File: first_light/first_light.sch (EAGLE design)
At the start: 20 parts, among them U1 STM32F051C6T6

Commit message: progress on schematic design
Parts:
- added C1, C2: (no value), rcl:C-EUC0603
- added C3, C4, C5: 100nF, rcl:C-EUC0603
- added IC1: MC34063AD, MC34063AD:MC34063AD
- added J1, J2: DCJ0202, con-jack:DCJ0202
- added JP1: PROG, pinhead:PINHD-1X5
- added LED1, LED2: (no value), led:LEDCHIP-LED0603
- added Q1: ZXMN4A06GTA, ZXMN4A06GTA:ZXMN4A06GTA
- added R14: 100R, rcl:R-EU_R0603
- added R15, R16: 10k, rcl:R-EU_R0603
- added R17, R18: 330, rcl:R-EU_R0603
- added S1: tact, SparkFun-Switches:MOMENTARY-SWITCH-SPST-PTH-6.0MM
- added S2: UP, SparkFun-Switches:MOMENTARY-SWITCH-SPST-PTH-6.0MM
- added S3: DOWN, SparkFun-Switches:MOMENTARY-SWITCH-SPST-PTH-6.0MM
- added S4: LEFT, SparkFun-Switches:MOMENTARY-SWITCH-SPST-PTH-6.0MM
- added S5: RIGHT, SparkFun-Switches:MOMENTARY-SWITCH-SPST-PTH-6.0MM
- added X1: 8MHz, IQD-Frequency-Products:CRYSTALS-NOGND-4-HSMX
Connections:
- new net !RST: JP1.1, S1.1, U1A.NRST
- new net +12V: J1.1, J2.1
- new net +3V3: C3.1, C4.1, C5.1, JP1.4, U1B.VDD, U1B.VDDA, U1B.VDD_2
- new net BTN_DN: S3.2, U1A.PA2
- new net BTN_L: S4.2, U1A.PA1
- new net BTN_R: S5.2, U1A.PA0
- new net BTN_UP: S2.2, U1A.PA3
- new net LED_ALM: R18.2, U1A.PA5
- new net LED_PWM: R14.1, R15.1
- new net LED_SET: R17.2, U1A.PA4
- new net N$14: C1.1, U1A.PF1-OSC_OUT, X1.1
- new net N$20: C2.1, U1A.PF0-OSC_IN, X1.2
- new net N$21: J2.2, J2.3, Q1.D_1, Q1.D_2
- new net N$23: Q1.G, R14.2
- new net N$24: LED2.A, R17.1
- new net N$25: R16.1, U1A.BOOT0
- new net N$26: LED1.A, R18.1
- new net SWCLK: JP1.3, U1A.PA14
- new net SWDIO: JP1.2, U1A.PA13
- net GND: now also C1.2, C2.2, C3.2, C4.2, C5.2, J1.2, J1.3, JP1.5, LED1.C, LED2.C, Q1.S, R15.2, R16.2, S1.2, S2.1, S3.1, S4.1, S5.1, U1B.VSS, U1B.VSSA, U1B.VSS_2
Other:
- note added: "Buck Converter"
- note added: "Display"
- note added: "LED Output"
- note added: "STM32"
- note added: "Supply"
- moved on the sheet: R1, R10, R11, R12, R13, R2, R3, R4, R5, R6, R7, R8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

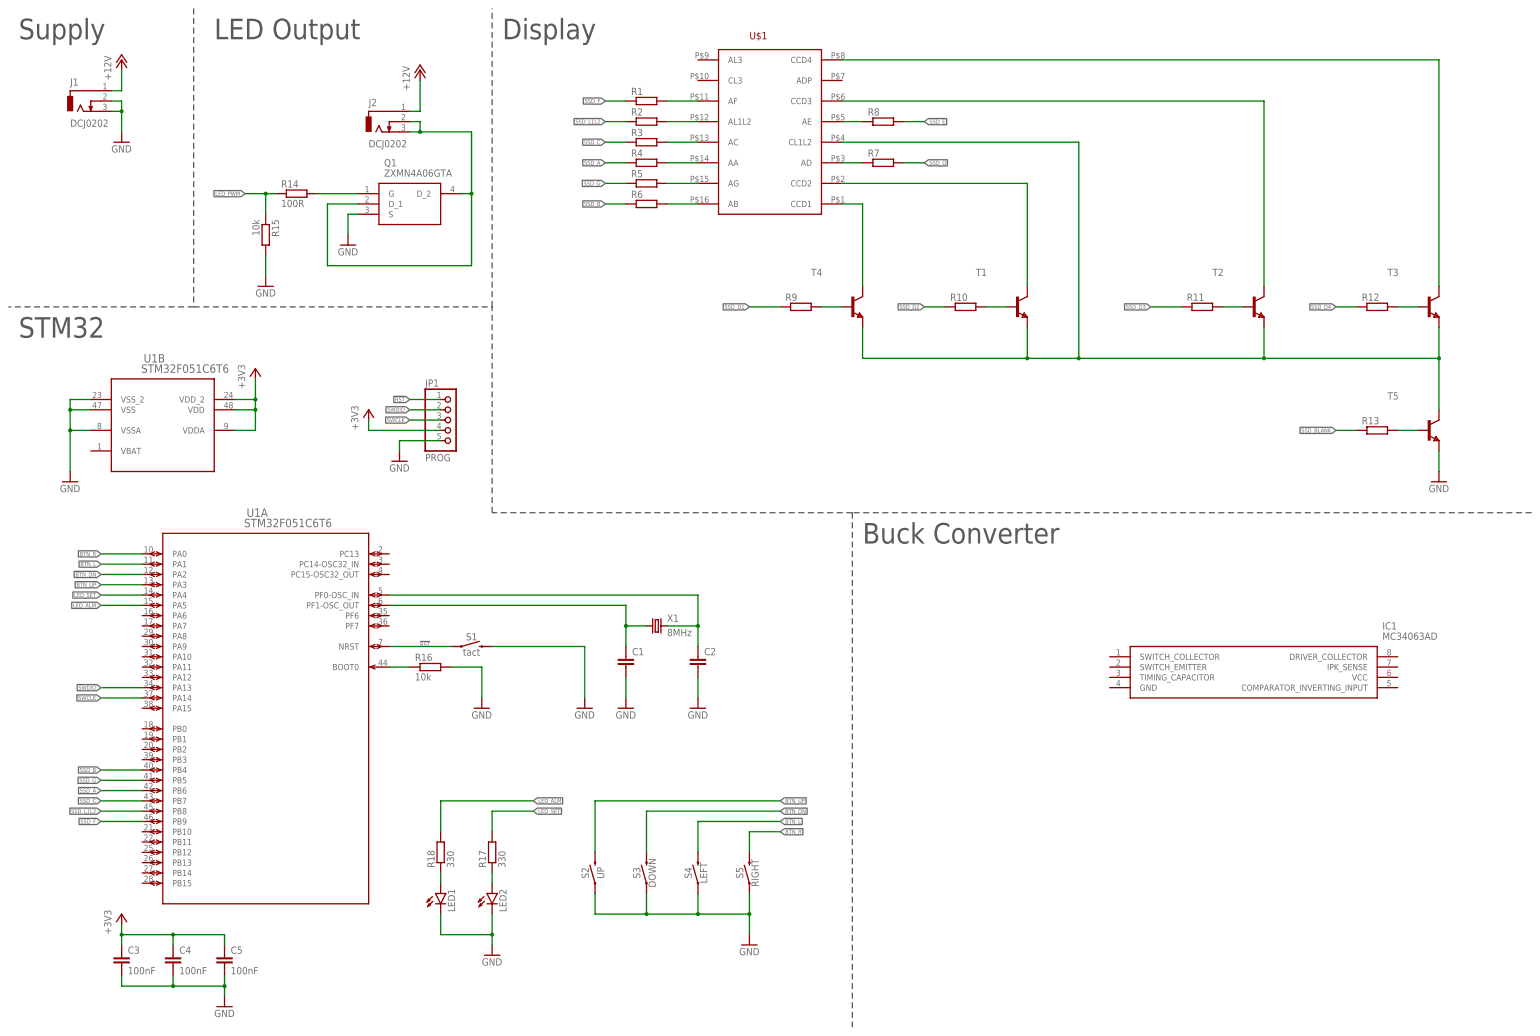
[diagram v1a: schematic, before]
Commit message: added buck regulator and fused input
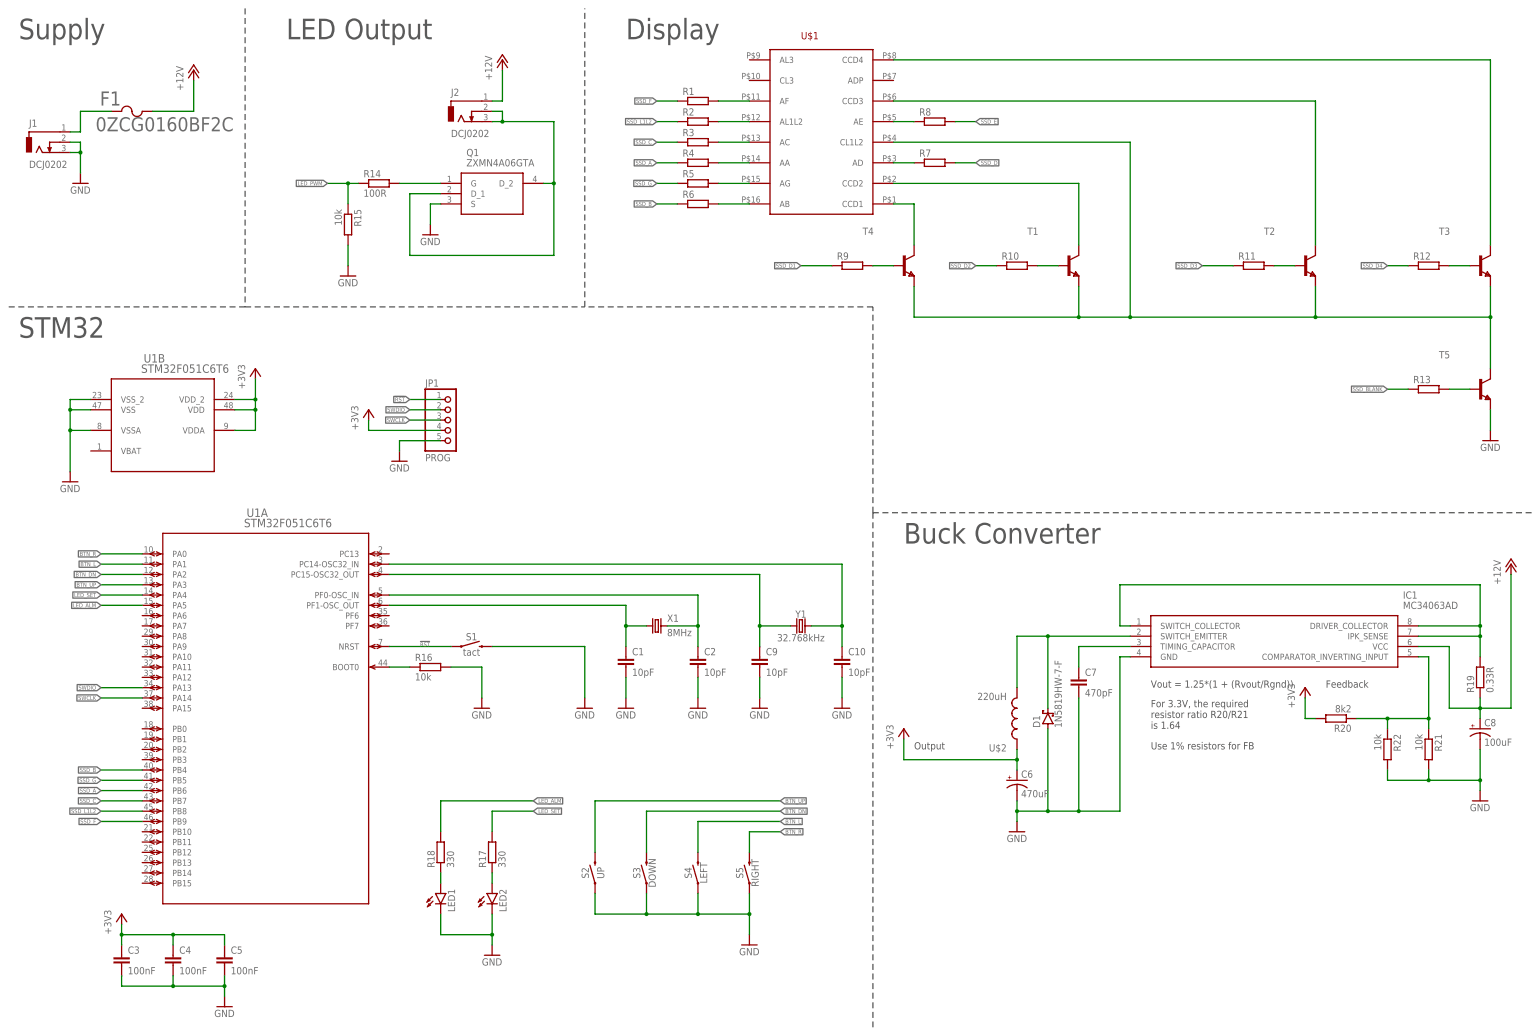
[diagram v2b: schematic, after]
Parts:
- added C10, C9: 10pF, rcl:C-EUC0603
- added C6: 470uF, rcl:CPOL-US153CLV-0605
- added C7: 470pF, rcl:C-EUC0603
- added C8: 100uF, rcl:CPOL-US153CLV-0605
- added D1: SCHOTTKY-1N5819HW-7-F, Schottky-1N5819HW-7-F:SCHOTTKY-1N5819HW-7-F
- added F1: 0ZCG0160BF2C, 0ZCG0160BF2C:0ZCG0160BF2C
- added R19: 0.33R, rcl:R-EU_R0603
- added R20: 8k2, rcl:R-EU_R0603
- added R21, R22: 10k, rcl:R-EU_R0603
- added U$2: 220uH, 1010_INDUCTOR:1010_INDUCTOR
- added Y1: 32.768kHz, SparkFun-Clocks:CRYSTAL-32.768KHZSMD-3.2X1.5
- C1, C2: value (none) -> 10pF
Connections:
- new net N$22: D1.C, IC1.SWITCH_EMITTER, U$2.2
- new net N$27: C7.1, IC1.TIMING_CAPACITOR
- new net N$28: IC1.DRIVER_COLLECTOR, IC1.IPK_SENSE, IC1.SWITCH_COLLECTOR, R19.2
- new net N$29: IC1.COMPARATOR_INVERTING_INPUT, R20.1, R21.1, R22.1
- new net N$30: C9.1, U1A.PC15-OSC32_OUT, Y1.1
- new net N$31: C10.1, U1A.PC14-OSC32_IN, Y1.2
- new net N$32: F1.1, J1.1
- net +12V: now also C8.+, F1.2, IC1.VCC, R19.1; no longer J1.1
- net +3V3: now also C6.+, R20.2, U$2.1
- net GND: now also C10.2, C6.-, C7.2, C8.-, C9.2, D1.A, IC1.GND, R21.2, R22.2
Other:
- note added: "Feedback"
- note added: "For 3.3V, the required resistor ratio R20/R21 is 1.64"
- note added: "Output"
- note added: "Use 1% resistors for FB"
- note added: "Vout = 1.25*(1 + (Rvout/Rgnd))"
- moved on the sheet: IC1, J1, J2, Q1, R1, R10, R11, R12, R13, R14, R15, R2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

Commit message: created a board and grouped parts by function
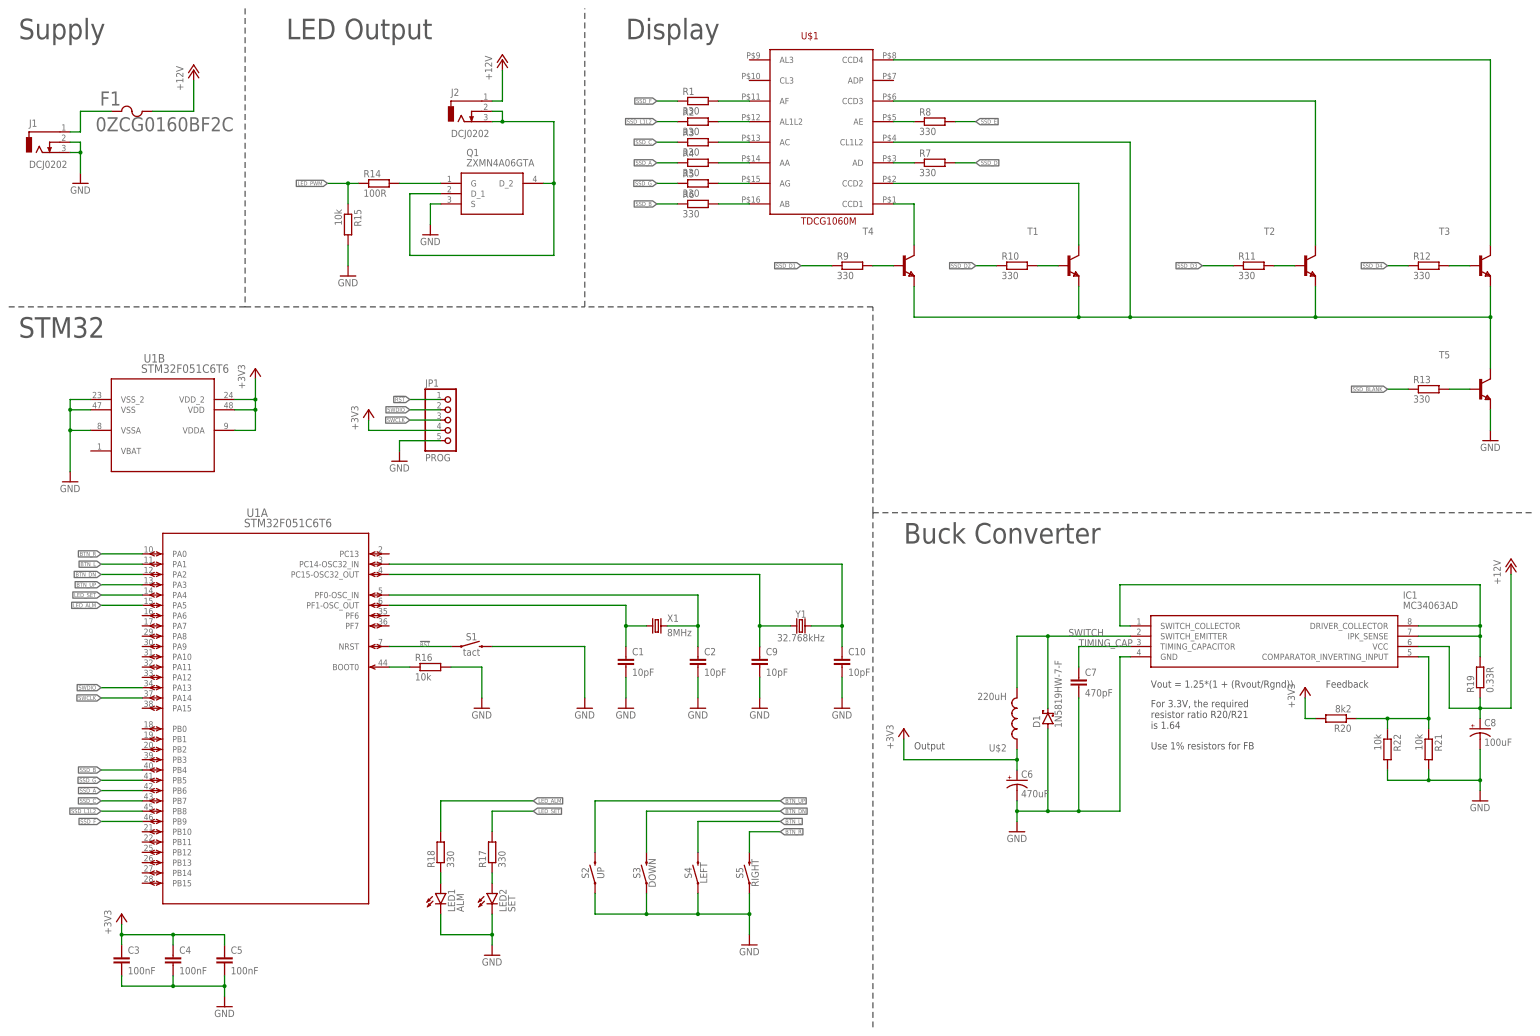
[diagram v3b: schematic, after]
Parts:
- LED1: value (none) -> ALM
- LED2: value (none) -> SET
- R1, R10, R11, R12, R13, R2, R3, R4, R5, R6, R7, R8, R9: value (none) -> 330
- U$1: value (none) -> TDCG1060M
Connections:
- net N$22 renamed SWITCH
- net N$27 renamed TIMING_CAP
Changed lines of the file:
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@@
 </classes>
 <parts>
-<part name="FRAME1" library="frames" library_urn="urn:adsk.eagle:library:229" deviceset="A3L-LOC" device=""/>
-<part name="U$1" library="TDCG1060M" deviceset="TDCG1060M" device=""/>
+<part name="FRAME1" library="frames" library_urn="urn:adsk.eagle:library:229" deviceset="A3L-LOC" device="" value="First Light Rev 2"/>
+<part name="U$1" library="TDCG1060M" deviceset="TDCG1060M" device="" value="TDCG1060M"/>
 <part name="U1" library="STM32F051C6" deviceset="STM32F051C6T6" device=""/>
-<part name="R1" library="rcl" library_urn="urn:adsk.eagle:library:334" deviceset="R-EU_" device="R0603" package3d_urn="urn:adsk.eagle:package:23555/3"/>
-<part name="R2" library="rcl" library_urn="urn:adsk.eagle:library:334" deviceset="R-EU_" device="R0603" package3d_urn="urn:adsk.eagle:package:23555/3"/>
-<part name="R3" library="rcl" library_urn="urn:adsk.eagle:library:334" deviceset="R-EU_" device="R0603" package3d_urn="urn:adsk.eagle:package:23555/3"/>
-<part name="R4" library="rcl" library_urn="urn:adsk.eagle:library:334" deviceset="R-EU_" device="R0603" package3d_urn="urn:adsk.eagle:package:23555/3"/>
-<part name="R5" library="rcl" library_urn="urn:adsk.eagle:library:334" deviceset="R-EU_" device="R0603" package3d_urn="urn:adsk.eagle:package:23555/3"/>
-<part name="R6" library="rcl" library_urn="urn:adsk.eagle:library:334" deviceset="R-EU_" device="R0603" package3d_urn="urn:adsk.eagle:package:23555/3"/>
-<part name="R7" library="rcl" library_urn="urn:adsk.eagle:library:334" deviceset="R-EU_" device="R0603" package3d_urn="urn:adsk.eagle:package:23555/3"/>
-<part name="R8" library="rcl" library_urn="urn:adsk.eagle:library:334" deviceset="R-EU_" device="R0603" package3d_urn="urn:adsk.eagle:package:23555/3"/>
+<part name="R1" library="rcl" library_urn="urn:adsk.eagle:library:334" deviceset="R-EU_" device="R0603" package3d_urn="urn:adsk.eagle:package:23555/3" value="330"/>
+<part name="R2" library="rcl" library_urn="urn:adsk.eagle:library:334" deviceset="R-EU_" device="R0603" package3d_urn="urn:adsk.eagle:package:23555/3" value="330"/>
+<part name="R3" library="rcl" library_urn="urn:adsk.eagle:library:334" deviceset="R-EU_" device="R0603" package3d_urn="urn:adsk.eagle:package:23555/3" value="330"/>
+<part name="R4" library="rcl" library_urn="urn:adsk.eagle:library:334" deviceset="R-EU_" device="R0603" package3d_urn="urn:adsk.eagle:package:23555/3" value="330"/>
+<part name="R5" library="rcl" library_urn="urn:adsk.eagle:library:334" deviceset="R-EU_" device="R0603" package3d_urn="urn:adsk.eagle:package:23555/3" value="330"/>
+<part name="R6" library="rcl" library_urn="urn:adsk.eagle:library:334" deviceset="R-EU_" device="R0603" package3d_urn="urn:adsk.eagle:package:23555/3" value="330"/>
+<part name="R7" library="rcl" library_urn="urn:adsk.eagle:library:334" deviceset="R-EU_" device="R0603" package3d_urn="urn:adsk.eagle:package:23555/3" value="330"/>
+<part name="R8" library="rcl" library_urn="urn:adsk.eagle:library:334" deviceset="R-EU_" device="R0603" package3d_urn="urn:adsk.eagle:package:23555/3" value="330"/>
 <part name="T1" library="zetex" library_urn="urn:adsk.eagle:library:418" deviceset="NPNSOT323" device="" package3d_urn="urn:adsk.eagle:package:30986/2"/>
 <part name="T2" library="zetex" library_urn="urn:adsk.eagle:library:418" deviceset="NPNSOT323" device="" package3d_urn="urn:adsk.eagle:package:30986/2"/>
@@
 <part name="T4" library="zetex" library_urn="urn:adsk.eagle:library:418" deviceset="NPNSOT323" device="" package3d_urn="urn:adsk.eagle:package:30986/2"/>
 <part name="T5" library="zetex" library_urn="urn:adsk.eagle:library:418" deviceset="NPNSOT323" device="" package3d_urn="urn:adsk.eagle:package:30986/2"/>
-<part name="R9" library="rcl" library_urn="urn:adsk.eagle:library:334" deviceset="R-EU_" device="R0603" package3d_urn="urn:adsk.eagle:package:23555/3"/>
-<part name="R10" library="rcl" library_urn="urn:adsk.eagle:library:334" deviceset="R-EU_" device="R0603" package3d_urn="urn:adsk.eagle:package:23555/3"/>
-<part name="R11" library="rcl" library_urn="urn:adsk.eagle:library:334" deviceset="R-EU_" device="R0603" package3d_urn="urn:adsk.eagle:package:23555/3"/>
-<part name="R12" library="rcl" library_urn="urn:adsk.eagle:library:334" deviceset="R-EU_" device="R0603" package3d_urn="urn:adsk.eagle:package:23555/3"/>
-<part name="R13" library="rcl" library_urn="urn:adsk.eagle:library:334" deviceset="R-EU_" device="R0603" package3d_urn="urn:adsk.eagle:package:23555/3"/>
+<part name="R9" library="rcl" library_urn="urn:adsk.eagle:library:334" deviceset="R-EU_" device="R0603" package3d_urn="urn:adsk.eagle:package:23555/3" value="330"/>
+<part name="R10" library="rcl" library_urn="urn:adsk.eagle:library:334" deviceset="R-EU_" device="R0603" package3d_urn="urn:adsk.eagle:package:23555/3" value="330"/>
+<part name="R11" library="rcl" library_urn="urn:adsk.eagle:library:334" deviceset="R-EU_" device="R0603" package3d_urn="urn:adsk.eagle:package:23555/3" value="330"/>
+<part name="R12" library="rcl" library_urn="urn:adsk.eagle:library:334" deviceset="R-EU_" device="R0603" package3d_urn="urn:adsk.eagle:package:23555/3" value="330"/>
+<part name="R13" library="rcl" library_urn="urn:adsk.eagle:library:334" deviceset="R-EU_" device="R0603" package3d_urn="urn:adsk.eagle:package:23555/3" value="330"/>
 <part name="GND1" library="supply1" library_urn="urn:adsk.eagle:library:371" deviceset="GND" device=""/>
 <part name="X1" library="IQD-Frequency-Products" library_urn="urn:adsk.eagle:library:90" deviceset="CRYSTALS-NOGND" device="-4-HSMX" package3d_urn="urn:adsk.eagle:package:3355/1" value="8MHz"/>
@@
 <part name="S5" library="SparkFun-Switches" library_urn="urn:adsk.eagle:library:535" deviceset="MOMENTARY-SWITCH-SPST" device="-PTH-6.0MM" package3d_urn="urn:adsk.eagle:package:40163/1" value="RIGHT"/>
 <part name="GND11" library="supply1" library_urn="urn:adsk.eagle:library:371" deviceset="GND" device=""/>
-<part name="LED1" library="led" library_urn="urn:adsk.eagle:library:259" deviceset="LED" device="CHIP-LED0603" package3d_urn="urn:adsk.eagle:package:15819/3"/>
-<part name="LED2" library="led" library_urn="urn:adsk.eagle:library:259" deviceset="LED" device="CHIP-LED0603" package3d_urn="urn:adsk.eagle:package:15819/3"/>
+<part name="LED1" library="led" library_urn="urn:adsk.eagle:library:259" deviceset="LED" device="CHIP-LED0603" package3d_urn="urn:adsk.eagle:package:15819/3" value="ALM"/>
+<part name="LED2" library="led" library_urn="urn:adsk.eagle:library:259" deviceset="LED" device="CHIP-LED0603" package3d_urn="urn:adsk.eagle:package:15819/3" value="SET"/>
 <part name="R17" library="rcl" library_urn="urn:adsk.eagle:library:334" deviceset="R-EU_" device="R0603" package3d_urn="urn:adsk.eagle:package:23555/3" value="330"/>
 <part name="R18" library="rcl" library_urn="urn:adsk.eagle:library:334" deviceset="R-EU_" device="R0603" package3d_urn="urn:adsk.eagle:package:23555/3" value="330"/>
@@
 </segment>
 </net>
-<net name="N$22" class="0">
+<net name="SWITCH" class="0">
 <segment>
 <pinref part="IC1" gate="G$1" pin="SWITCH_EMITTER"/>
@@
 <wire x1="261.62" y1="83.82" x2="261.62" y2="101.6" width="0.1524" layer="91"/>
 <junction x="261.62" y="101.6"/>
-</segment>
-</net>
-<net name="N$27" class="0">
+<label x="266.7" y="101.6" size="1.778" layer="95"/>
+</segment>
+</net>
+<net name="TIMING_CAP" class="0">
 <segment>
 <pinref part="IC1" gate="G$1" pin="TIMING_CAPACITOR"/>
@@
 <pinref part="C7" gate="G$1" pin="1"/>
 <wire x1="269.24" y1="99.06" x2="269.24" y2="93.98" width="0.1524" layer="91"/>
+<label x="269.24" y="99.06" size="1.778" layer="95"/>
 </segment>
 </net>
@@
 </sheet>
 </sheets>
+<errors>
+</errors>
 </schematic>
 </drawing>
